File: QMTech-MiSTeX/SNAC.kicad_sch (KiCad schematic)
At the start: 14 parts

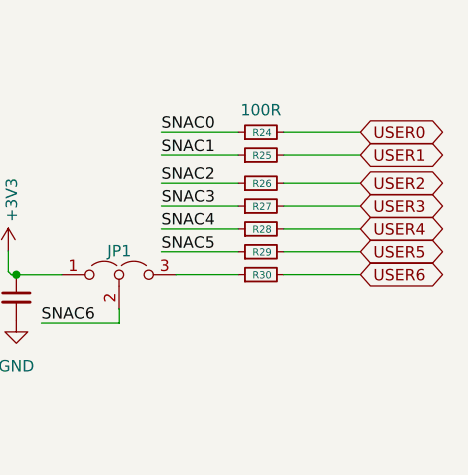
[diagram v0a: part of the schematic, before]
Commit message: fix SNAC pinout to match with the mapping described in sys/mt32pi.v
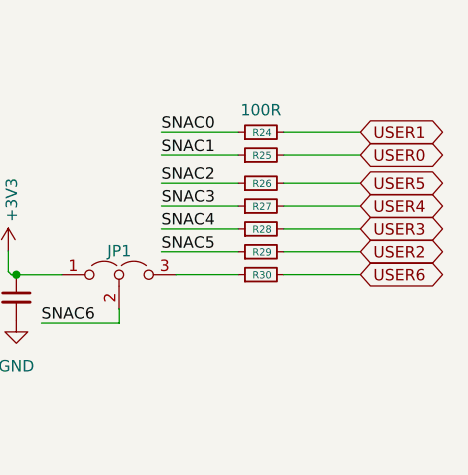
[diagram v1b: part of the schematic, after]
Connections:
- net USER0: now also R25.2; no longer R24.2
- net USER1: now also R24.2; no longer R25.2
- net USER2: now also R29.2; no longer R26.2
- net USER3: now also R28.2; no longer R27.2
- net USER4: now also R27.2; no longer R28.2
- net USER5: now also R26.2; no longer R29.2
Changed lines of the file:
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@@
     (effects (font (size 1.27 1.27)) (justify right bottom))
   )
-  (global_label "USER2" (shape bidirectional) (at 153.6757 88.9787 0) (fields_autoplaced)
+  (global_label "USER2" (shape bidirectional) (at 153.6757 96.5987 0) (fields_autoplaced)
     (effects (font (size 1.27 1.27)) (justify left))
-    (property "Intersheetrefs" "${INTERSHEET_REFS}" (at 163.9405 88.9787 0)
+    (property "Intersheetrefs" "${INTERSHEET_REFS}" (at 163.9405 96.5987 0)
       (effects (font (size 1.27 1.27)) (justify left))
     )
@@
     )
   )
-  (global_label "USER1" (shape bidirectional) (at 153.6757 85.852 0) (fields_autoplaced)
+  (global_label "USER1" (shape bidirectional) (at 153.6757 83.312 0) (fields_autoplaced)
+    (effects (font (size 1.27 1.27)) (justify left))
+    (property "Intersheetrefs" "${INTERSHEET_REFS}" (at 163.9405 83.312 0)
+      (effects (font (size 1.27 1.27)) (justify left))
+    )
+  )
+  (global_label "USER0" (shape bidirectional) (at 153.6757 85.852 0) (fields_autoplaced)
     (effects (font (size 1.27 1.27)) (justify left))
     (property "Intersheetrefs" "${INTERSHEET_REFS}" (at 163.9405 85.852 0)
@@
     )
   )
-  (global_label "USER0" (shape bidirectional) (at 153.6757 83.312 0) (fields_autoplaced)
+  (global_label "USER3" (shape bidirectional) (at 153.6757 94.0587 0) (fields_autoplaced)
     (effects (font (size 1.27 1.27)) (justify left))
-    (property "Intersheetrefs" "${INTERSHEET_REFS}" (at 163.9405 83.312 0)
+    (property "Intersheetrefs" "${INTERSHEET_REFS}" (at 163.9405 94.0587 0)
       (effects (font (size 1.27 1.27)) (justify left))
     )
   )
-  (global_label "USER3" (shape bidirectional) (at 153.6757 91.5187 0) (fields_autoplaced)
+  (global_label "USER5" (shape bidirectional) (at 153.6757 88.9787 0) (fields_autoplaced)
+    (effects (font (size 1.27 1.27)) (justify left))
+    (property "Intersheetrefs" "${INTERSHEET_REFS}" (at 163.9405 88.9787 0)
+      (effects (font (size 1.27 1.27)) (justify left))
+    )
+  )
+  (global_label "USER4" (shape bidirectional) (at 153.6757 91.5187 0) (fields_autoplaced)
     (effects (font (size 1.27 1.27)) (justify left))
     (property "Intersheetrefs" "${INTERSHEET_REFS}" (at 163.9405 91.5187 0)
       (effects (font (size 1.27 1.27)) (justify left))
     )
-  )
-  (global_label "USER5" (shape bidirectional) (at 153.6757 96.5987 0) (fields_autoplaced)
-    (effects (font (size 1.27 1.27)) (justify left))
-    (property "Intersheetrefs" "${INTERSHEET_REFS}" (at 163.9405 96.5987 0)
-      (effects (font (size 1.27 1.27)) (justify left))
-    )
-  )
-  (global_label "USER4" (shape bidirectional) (at 153.6757 94.0587 0) (fields_autoplaced)
-    (effects (font (size 1.27 1.27)) (justify left))
-    (property "Intersheetrefs" "${INTERSHEET_REFS}" (at 163.9405 94.0587 0)
-      (effects (font (size 1.27 1.27)) (justify left))
-    )

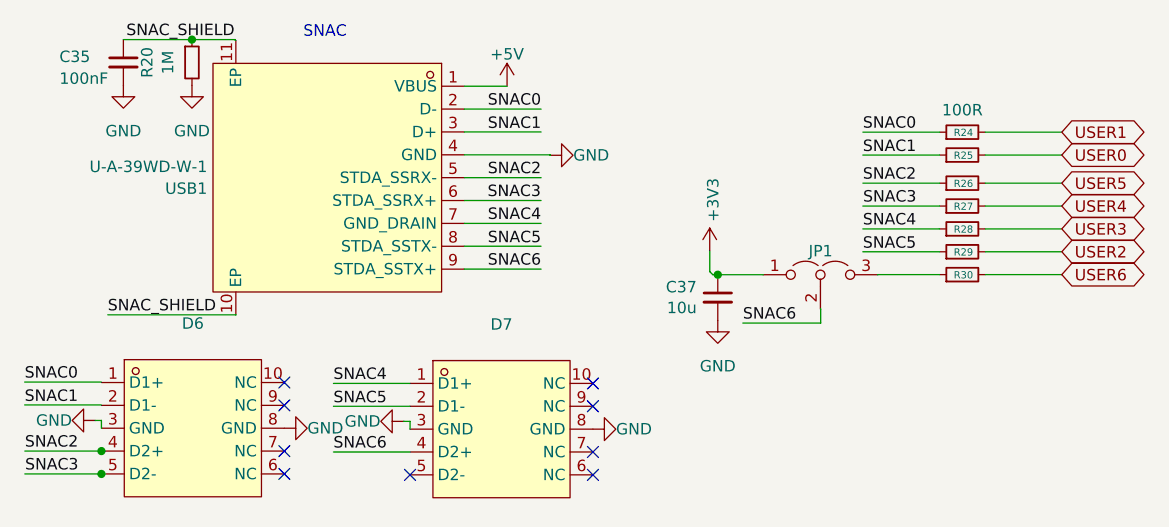
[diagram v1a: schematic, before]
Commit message: apply review notes from somhi, move audio into its own subsheet, add analog audio out
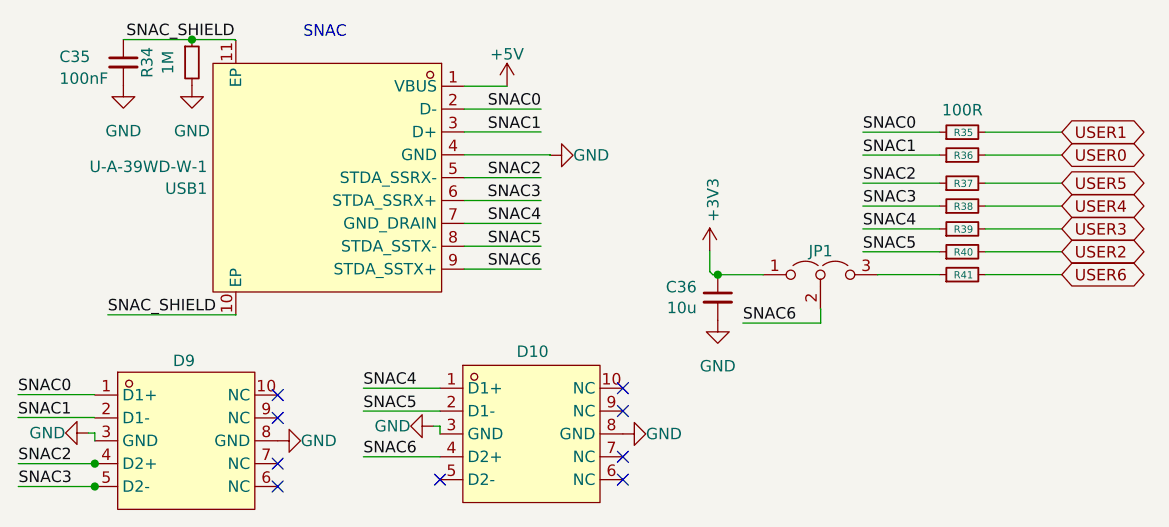
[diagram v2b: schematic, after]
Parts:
- renumbered C37 to C36, D7 to D10, D6 to D9, R20 to R34, R24 to R35, R25 to R36, R26 to R37, R27 to R38, R28 to R39, R29 to R40, R30 to R41
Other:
- moved on the sheet: D10, D9

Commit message: finish routing/layouting, fix silk screen, add mounting holes
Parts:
- removed C35: 100nF, C_0402_1005Metric, symbol jlcpcb-basic-mlcc-0402:100nF
- removed C36: 10u, Capacitor_SMD:C_0603_1608Metric, symbol Device:C_Small
- removed D10, D9: TPD4E05U06DQAR_C2972498, easyeda2kicad:DFN2510-10_L2.5-W1.0-P0.50-BL, symbol easyeda2kicad:TPD4E05U06DQAR_C2972498
- removed JP1: Jumper_3_Open, Connector_PinHeader_2.54mm:PinHeader_1x03_P2.54mm_Vertical, symbol Jumper:Jumper_3_Open
- removed R34: 1M, Resistor_SMD:R_0603_1608Metric, symbol Device:R_Small
- removed R35, R36, R37, R38, R39, R40, R41: 100R, R_0402_1005Metric, symbol jlcpcb-basic-resistor-0402:100R
- removed USB1: U-A-39WD-W-1, easyeda2kicad:USB-A-SMD_U-A-39WD-W-1, symbol easyeda2kicad:U-A-39WD-W-1
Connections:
- no-connect marks 9 -> 0
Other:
- note removed: "SNAC"
